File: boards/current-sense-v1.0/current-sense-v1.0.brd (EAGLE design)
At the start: 71.5 x 95.6 mm, 89 parts, among them IC1 ISO7241, IC2 ISO7241, IC3 ISO7242, IC4 ISO7240, J1 4-PIN_2MM-H, J2 MKS-1658, J3 8-PIN_2MM-H, J6 DF22-2, Q1 IRFH7545, Q2 IRFH7545, Q3 IRFH7545, Q4 IRFH7545, Q5 IRFH7545, Q6 IRFH7545, U1 DRV8303DCA, U13 TLV70233DBVR, U2 INA240PWR, U3 INA240PWR, U4 INA240PWR, U6 ADS8028IRTJT, U7 MPM3620GQV-P, U8 VND5E006ASPTR-E, U9 TLV70450

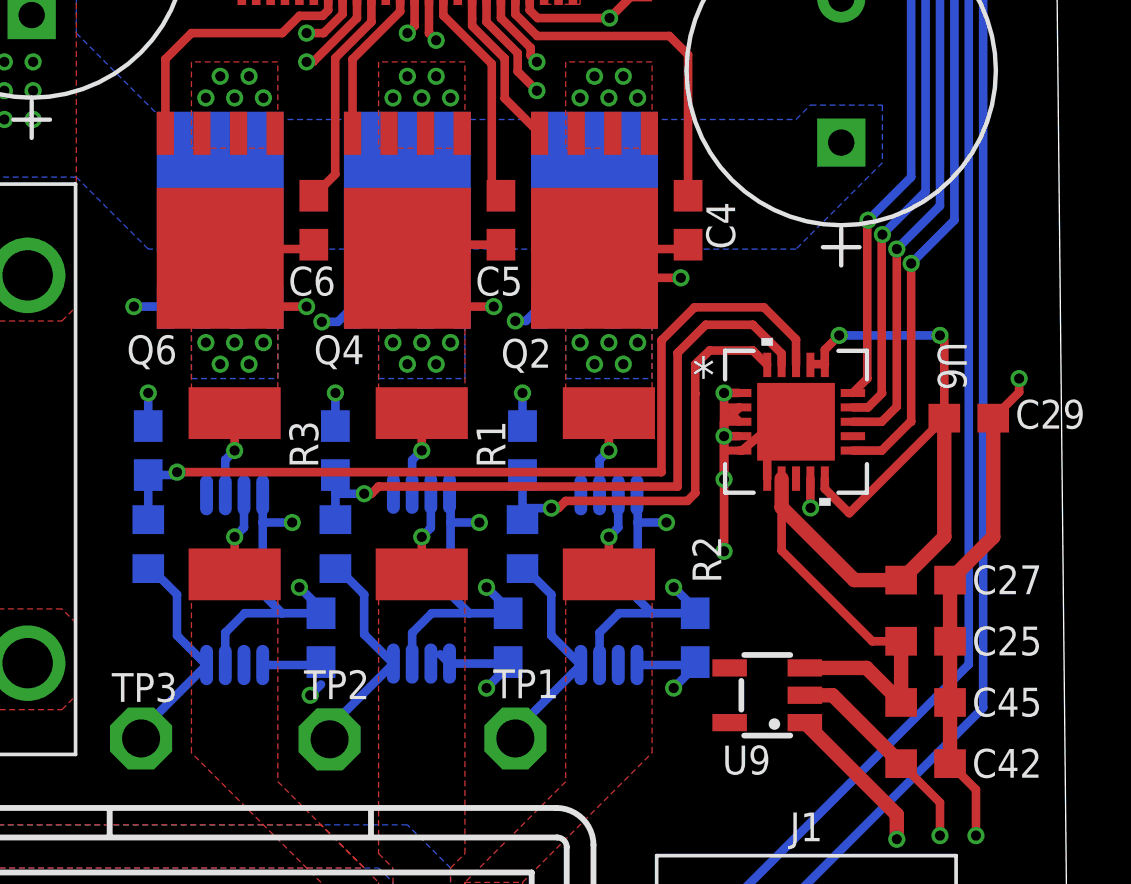
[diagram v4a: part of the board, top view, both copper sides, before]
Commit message: fixed clearances and resized some wires from 0.5 to 0.3
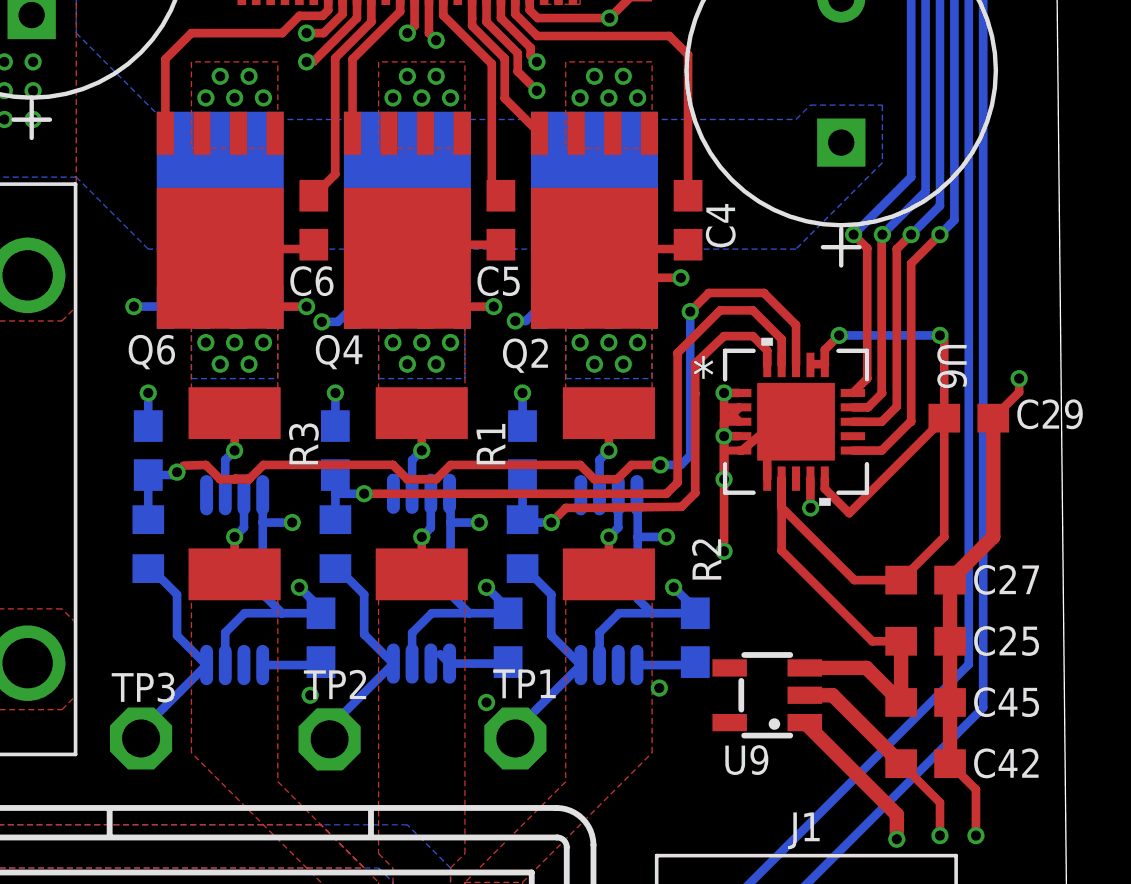
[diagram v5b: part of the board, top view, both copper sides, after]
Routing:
- net +5V: track 149.2 -> 146.4 mm
- net SENSE_C: track 30.5 -> 33.2 mm, vias 1 -> 3
- net SENSE_A: track 15.2 -> 16.1 mm
- net SENSE_B: track 23.0 -> 23.6 mm

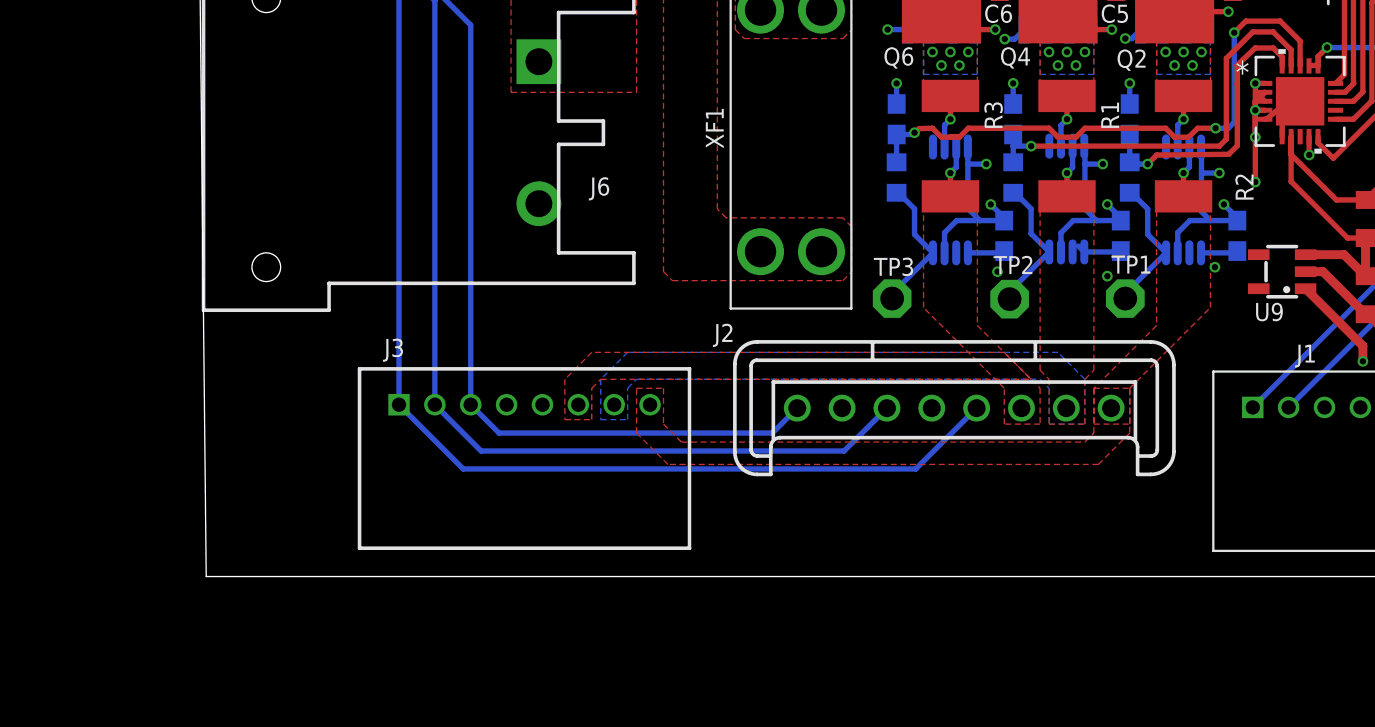
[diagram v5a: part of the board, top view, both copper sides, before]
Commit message: added borders in board view
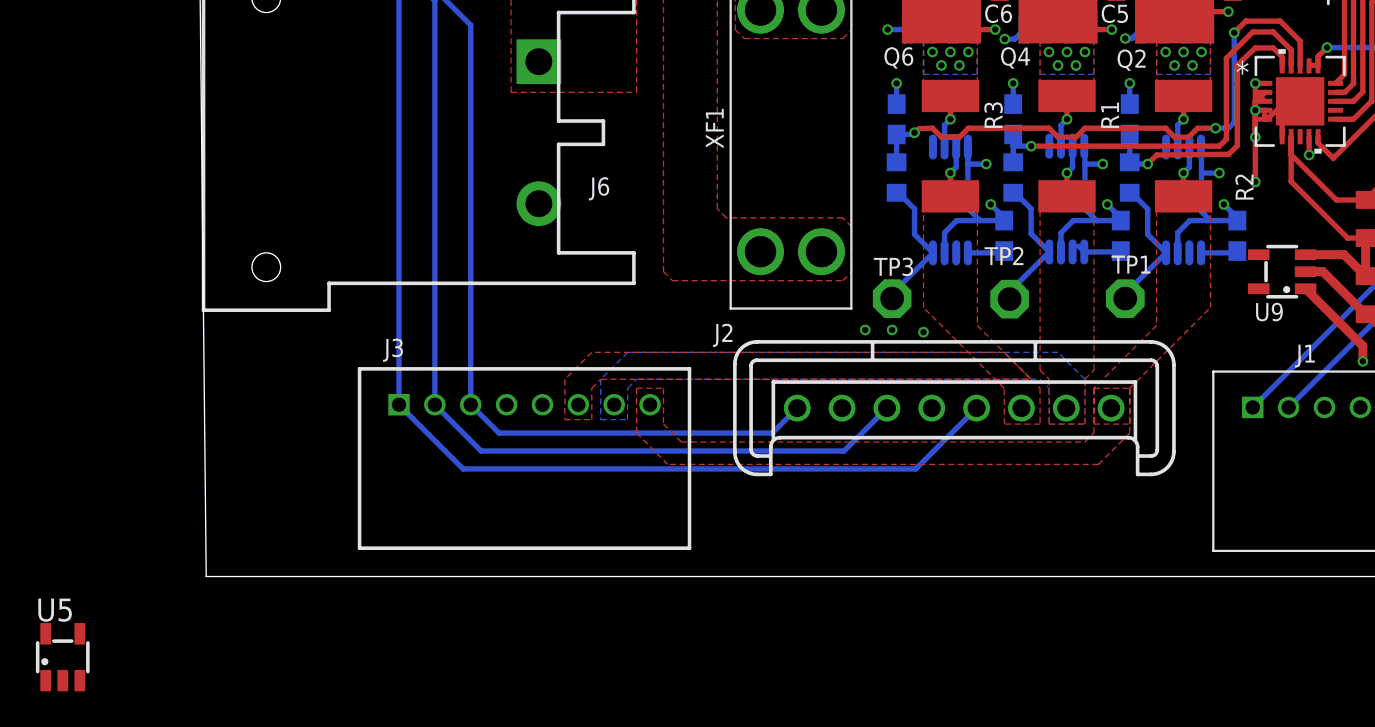
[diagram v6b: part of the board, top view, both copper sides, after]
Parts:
- added U5: TLV70233DBVR, RoboJackets-PowerICs:SOT-23-5
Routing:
- net +5V: track 146.4 -> 132.7 mm
- net GND: track 197.4 -> 197.9 mm
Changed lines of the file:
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@@
 </element>
 <element name="TP2" library="testpad" library_urn="urn:adsk.eagle:library:385" package="P1-13" package3d_urn="urn:adsk.eagle:package:27946/1" value="PTR1PAD1-13" x="45.3" y="10.47" smashed="yes">
-<attribute name="NAME" x="44.409" y="11.865" size="1" layer="25" ratio="10"/>
+<attribute name="NAME" x="43.909" y="12.365" size="1" layer="25" ratio="10"/>
 <attribute name="TP_SIGNAL_NAME" value="" x="44.03" y="7.93" size="1" layer="37"/>
 <attribute name="VALUE" x="45.3" y="9.97" size="0.0254" layer="27"/>
@@
 <attribute name="NAME" x="3.51" y="66.24" size="1" layer="25" rot="R180"/>
 <attribute name="VALUE" x="2.885" y="66.405" size="1.27" layer="27" rot="R180"/>
+</element>
+<element name="U5" library="RoboJackets-PowerICs" package="SOT-23-5" value="TLV70233DBVR" x="-7.5" y="-9.5" smashed="yes">
+<attribute name="DIGIKEY" value="296-32415-1-ND" x="-7.5" y="-9.5" size="1.778" layer="27" display="off"/>
+<attribute name="MPN" value="TLV70233DBVR" x="-7.5" y="-9.5" size="1.778" layer="27" display="off"/>
+<attribute name="NAME" x="-9" y="-7.5" size="1.27" layer="25" ratio="10"/>
 </element>
 </elements>
@@
 <wire x1="62.000125" y1="18.5147" x2="62.0074125" y2="18.5074125" width="0.1524" layer="1"/>
 <via x="62.0074125" y="18.5074125" extent="1-16" drill="0.35"/>
-<wire x1="44.305" y1="58.9" x2="51.925" y2="58.9" width="0" layer="19" extent="1-1"/>
-<wire x1="43" y1="54.75" x2="44.25" y2="57.25" width="0" layer="19" extent="1-1"/>
-<wire x1="32.805" y1="58.9" x2="40.425" y2="58.9" width="0" layer="19" extent="1-1"/>
-<wire x1="30.25" y1="57.25" x2="32.75" y2="57.25" width="0" layer="19" extent="1-1"/>
-<wire x1="22.575" y1="58.9" x2="30.195" y2="58.9" width="0" layer="19" extent="1-1"/>
-<wire x1="15.25" y1="50" x2="18.75" y2="54.65" width="0" layer="19" extent="1-1"/>
-<wire x1="15.25" y1="49" x2="15.25" y2="50" width="0" layer="19" extent="1-1"/>
-<wire x1="13.95" y1="49.5" x2="15.25" y2="50" width="0" layer="19" extent="1-1"/>
-<wire x1="7.75" y1="47.75" x2="13.95" y2="49.5" width="0" layer="19" extent="1-1"/>
-<wire x1="6.5" y1="43.9" x2="7.25" y2="46.75" width="0" layer="19" extent="1-1"/>
-<wire x1="5.5" y1="41.5" x2="5" y2="43.9" width="0" layer="19" extent="1-1"/>
-<wire x1="4.5" y1="41.5" x2="5.5" y2="41.5" width="0" layer="19" extent="1-1"/>
-<wire x1="3.5" y1="41.5" x2="4.5" y2="41.5" width="0" layer="19" extent="1-1"/>
-<wire x1="2.5" y1="41.5" x2="3.5" y2="41.5" width="0" layer="19" extent="1-1"/>
-<wire x1="5.55" y1="49.75" x2="7.75" y2="47.75" width="0" layer="19" extent="1-1"/>
-<wire x1="5.55" y1="50.25" x2="5.55" y2="49.75" width="0" layer="19" extent="1-1"/>
-<wire x1="6.45" y1="50.45" x2="5.55" y2="50.25" width="0" layer="19" extent="1-1"/>
-<wire x1="5.5" y1="51.75" x2="5.55" y2="50.25" width="0" layer="19" extent="1-1"/>
-<wire x1="4.5" y1="51.75" x2="5.5" y2="51.75" width="0" layer="19" extent="1-1"/>
-<wire x1="3.5" y1="51.75" x2="4.5" y2="51.75" width="0" layer="19" extent="1-1"/>
-<wire x1="3.5" y1="50.6" x2="3.5" y2="51.75" width="0" layer="19" extent="1-1"/>
-<wire x1="1.5" y1="54.5" x2="3.5" y2="51.75" width="0" layer="19" extent="1-1"/>
-<wire x1="9" y1="40.185" x2="5.5" y2="41.5" width="0" layer="19" extent="1-1"/>
-<wire x1="9.75" y1="57.25" x2="5.5" y2="51.75" width="0" layer="19" extent="1-1"/>
-<wire x1="13" y1="34.5" x2="9" y2="40.185" width="0" layer="19" extent="1-1"/>
-<wire x1="11" y1="33" x2="13" y2="34.5" width="0" layer="19" extent="1-1"/>
-<wire x1="19.5" y1="42" x2="19.35" y2="37.125" width="0" layer="19" extent="16-16"/>
-<wire x1="22" y1="41.5" x2="19.5" y2="42" width="0" layer="19" extent="1-1"/>
-<wire x1="52.75" y1="44.25" x2="54.5" y2="54.5" width="0" layer="19" extent="1-1"/>
-<wire x1="47" y1="40.5" x2="48" y2="40.5" width="0" layer="19" extent="1-1"/>
-<wire x1="53.35" y1="42" x2="52.75" y2="44.25" width="0" layer="19" extent="1-16"/>
-<wire x1="53.75" y1="36.75" x2="56" y2="38.35" width="0" layer="19" extent="1-1"/>
-<wire x1="53.25" y1="36.75" x2="53.75" y2="36.75" width="0" layer="19" extent="1-1"/>
-<wire x1="52.75" y1="36.75" x2="53.25" y2="36.75" width="0" layer="19" extent="1-1"/>
-<wire x1="54.5" y1="33.5" x2="53.75" y2="36.75" width="0" layer="19" extent="1-1"/>
-<wire x1="54" y1="32.75" x2="54.5" y2="33.5" width="0" layer="19" extent="1-1"/>
-<wire x1="55" y1="32.75" x2="54.5" y2="33.5" width="0" layer="19" extent="1-1"/>
-<wire x1="55.5" y1="33.5" x2="55" y2="32.75" width="0" layer="19" extent="1-1"/>
-<wire x1="56" y1="32.75" x2="55.5" y2="33.5" width="0" layer="19" extent="1-1"/>
-<wire x1="55.135" y1="31.52" x2="55" y2="32.75" width="0" layer="19" extent="1-1"/>
-<wire x1="53.865" y1="31.52" x2="54" y2="32.75" width="0" layer="19" extent="1-1"/>
-<wire x1="56.405" y1="31.52" x2="55.135" y2="31.52" width="0" layer="19" extent="1-1"/>
-<wire x1="49" y1="33.5" x2="49.75" y2="36.75" width="0" layer="19" extent="1-1"/>
-<wire x1="48.5" y1="32.75" x2="49" y2="33.5" width="0" layer="19" extent="1-1"/>
-<wire x1="48" y1="33.5" x2="48.5" y2="32.75" width="0" layer="19" extent="1-1"/>
-<wire x1="49.5" y1="32.75" x2="49" y2="33.5" width="0" layer="19" extent="1-1"/>
-<wire x1="47.5" y1="32.75" x2="48" y2="33.5" width="0" layer="19" extent="1-1"/>
-<wire x1="48.635" y1="31.52" x2="48.5" y2="32.75" width="0" layer="19" extent="1-1"/>
-<wire x1="47.365" y1="31.52" x2="47.5" y2="32.75" width="0" layer="19" extent="1-1"/>
-<wire x1="49.905" y1="31.52" x2="48.635" y2="31.52" width="0" layer="19" extent="1-1"/>
-<wire x1="43.405" y1="31.52" x2="47.365" y2="31.52" width="0" layer="19" extent="1-1"/>
-<wire x1="42.135" y1="31.52" x2="43.405" y2="31.52" width="0" layer="19" extent="1-1"/>
-<wire x1="42" y1="32.75" x2="42.135" y2="31.52" width="0" layer="19" extent="1-1"/>
-<wire x1="41.5" y1="33.5" x2="42" y2="32.75" width="0" layer="19" extent="1-1"/>
-<wire x1="42.5" y1="33.5" x2="42" y2="32.75" width="0" layer="19" extent="1-1"/>
-<wire x1="43" y1="32.75" x2="42.5" y2="33.5" width="0" layer="19" extent="1-1"/>
-<wire x1="41" y1="32.75" x2="41.5" y2="33.5" width="0" layer="19" extent="1-1"/>
-<wire x1="40.865" y1="31.52" x2="41" y2="32.75" width="0" layer="19" extent="1-1"/>
-<wire x1="63.07" y1="36.2" x2="56" y2="38.35" width="0" layer="19" extent="1-1"/>
-<wire x1="34.95" y1="40.63" x2="42.375" y2="40.15" width="0" layer="19" extent="16-16"/>
-<wire x1="52" y1="22.5" x2="53.865" y2="31.52" width="0" layer="19" extent="1-1"/>
-<wire x1="49.465003125" y1="19.000003125" x2="52" y2="21.35" width="0" layer="19" extent="16-16"/>
-<wire x1="45" y1="14.85" x2="48.165003125" y2="13.1" width="0" layer="19" extent="16-16"/>
-<wire x1="45.5" y1="21.35" x2="42.975003125" y2="18.950003125" width="0" layer="19" extent="16-16"/>
-<wire x1="54.675003125" y1="13.05" x2="51.5" y2="14.85" width="0" layer="19" extent="16-16"/>
-<wire x1="59" y1="17" x2="57.25" y2="15.75" width="0" layer="19" extent="1-1"/>
-<wire x1="59.525" y1="20.5" x2="59.525" y2="21" width="0" layer="19" extent="1-1"/>
-<wire x1="61.5" y1="21.5" x2="61.456621875" y2="22.043378125" width="0" layer="19" extent="1-1"/>
+<wire x1="59.525" y1="21" x2="59.525" y2="20.5" width="0.3" layer="1"/>
+<wire x1="61.456621875" y1="22.043378125" x2="61.5" y2="21.5" width="0" layer="19" extent="1-1"/>
 <wire x1="62.5" y1="22" x2="61.456621875" y2="22.043378125" width="0" layer="19" extent="1-1"/>
-<wire x1="62.000125" y1="19.525" x2="60.499746875" y2="19.525" width="0" layer="19" extent="1-1"/>
-<wire x1="39" y1="21.35" x2="42.975003125" y2="18.950003125" width="0" layer="19" extent="16-16"/>
-<wire x1="61.806" y1="11.05" x2="58" y2="14.85" width="0" layer="19" extent="1-16"/>
-<wire x1="67.75" y1="7.125" x2="65" y2="7" width="0" layer="19" extent="1-1"/>
-<wire x1="62.86" y1="4.43" x2="65" y2="7" width="0" layer="19" extent="1-1"/>
-<wire x1="35.96" y1="4.39" x2="41.675003125" y2="13.05" width="0" layer="19" extent="16-16"/>
-<wire x1="19.05" y1="15.79" x2="19.35" y2="32.875" width="0" layer="19" extent="16-16"/>
-<wire x1="17.25" y1="4.58" x2="19.05" y2="15.79" width="0" layer="19" extent="1-1"/>
 </signal>
 <signal name="PHASE_A">
@@
 <wire x1="23.65" y1="44" x2="24.5" y2="44.85" width="0.5" layer="1"/>
 <wire x1="21.5" y1="44" x2="23.65" y2="44" width="0.5" layer="1"/>
-<via x="44.625" y="12" extent="1-16" drill="0.35"/>
-<via x="50.75" y="11.75" extent="1-16" drill="0.35"/>
-<via x="56.75" y="12.25" extent="1-16" drill="0.35"/>
+<via x="40.5" y="8.625" extent="1-16" drill="0.35"/>
+<via x="38.75" y="8.75" extent="1-16" drill="0.35"/>
+<via x="37.25" y="8.75" extent="1-16" drill="0.35"/>
 <via x="15.25" y="47.5" extent="1-16" drill="0.35"/>
 <via x="15.25" y="46.5" extent="1-16" drill="0.35"/>
@@
 <wire x1="40.96" y1="4.39" x2="40.96" y2="6.96" width="0.5" layer="3"/>
 <wire x1="40.96" y1="6.96" x2="41" y2="7" width="0.5" layer="3"/>
-<wire x1="50.5" y1="12" x2="50.75" y2="11.75" width="0.5" layer="3"/>
-<wire x1="50.5" y1="12" x2="44.625" y2="12" width="0.5" layer="3"/>
-<wire x1="56.75" y1="12.25" x2="51.25" y2="12.25" width="0.5" layer="3"/>
-<wire x1="51.25" y1="12.25" x2="50.75" y2="11.75" width="0.5" layer="3"/>
-<wire x1="56.75" y1="12.25" x2="60" y2="9" width="0.5" layer="3"/>
-<wire x1="60" y1="9" x2="60" y2="7" width="0.5" layer="3"/>
+<wire x1="40.96" y1="8.39" x2="40.725" y2="8.625" width="0.5" layer="3"/>
+<wire x1="40.725" y1="8.625" x2="40.5" y2="8.625" width="0.5" layer="3"/>
+<wire x1="40.5" y1="8.625" x2="40" y2="8.625" width="0.5" layer="3"/>
+<wire x1="40" y1="8.625" x2="39.875" y2="8.75" width="0.5" layer="3"/>
+<wire x1="39.875" y1="8.75" x2="38.75" y2="8.75" width="0.5" layer="3"/>
+<wire x1="38.75" y1="8.75" x2="37.25" y2="8.75" width="0.5" layer="3"/>
+<wire x1="41" y1="7" x2="41" y2="8.35" width="0.5" layer="3"/>
+<wire x1="41" y1="8.35" x2="40.96" y2="8.39" width="0.1524" layer="3"/>
 <wire x1="15.25" y1="47.5" x2="14.1" y2="47" width="0" layer="19" extent="1-1"/>
 </signal>
